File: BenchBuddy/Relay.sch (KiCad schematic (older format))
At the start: 0 parts

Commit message: Week3 part 1
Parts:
- added D?: LED, ~, symbol LED
- added D?: DIODE, ~, symbol DIODE
- added K?: RELAY_SPDT, ~, symbol RELAY_SPDT
- added Q?: NPN, ~, symbol NPN
- added R? (x5): R, ~, symbol R
- added U?: PHTRANS, ~, symbol PHTRANS
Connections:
- net DIN+: now also U?.1
- net DIN-: now also R?.1
- new net: R?.2, U?.2
- new net: D?.1 (A), R?.1, U?.4
- new net: R?.1, U?.6
- new net: Q?.1 (E), R?.1
- new net: Q?.2 (B), R?.2
- new net: D?.1 (A), K?.5 (COIL_-), Q?.3 (C)
- new net: D?.2 (K), R?.1
- new net +12P: D?.2 (K), K?.2 (COIL_+), R?.2, U?.5
- new net COM: K?.1 (COM)
- new net GND: R?.2, R?.2
- new net NC: K?.4 (NC)
- new net NO: K?.3 (NO)
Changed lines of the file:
@@
 $Descr A4 11693 8268
 encoding utf-8
-Sheet 4 8
+Sheet 4 9
 Title ""
-Date "1 feb 2014"
+Date "5 mar 2014"
 Rev ""
 Comp ""
@@
 Comment4 ""
 $EndDescr
-Text HLabel 1100 1400 0    60   Input ~ 0
+Text HLabel 1550 3050 0    60   Input ~ 0
 DIN+
-Text HLabel 1100 1700 0    60   Output ~ 0
+Text HLabel 1550 3400 0    60   Output ~ 0
 DIN-
-Text HLabel 9850 1650 0    60   Input ~ 0
-Relay+
-Text HLabel 9850 1900 0    60   Output ~ 0
-Relay-
+Text HLabel 9450 1800 2    60   BiDi ~ 0
+NC
+Text HLabel 9450 2000 2    60   BiDi ~ 0
+NO
+$Comp
+L PHTRANS U?
+U 1 1 53162E90
+P 4200 3250
+F 0 "U?" H 4150 3600 70  0000 C CNN
+F 1 "PHTRANS" H 4150 2900 70  0000 C CNN
+F 2 "~" H 4200 3250 60  0000 C CNN
+F 3 "~" H 4200 3250 60  0000 C CNN
+	1    4200 3250
+	1    0    0    -1
+$EndComp
+$Comp
+L NPN Q?
+U 1 1 53162E9F
+P 8000 3450
+F 0 "Q?" H 8000 3300 50  0000 R CNN
+F 1 "NPN" H 8000 3600 50  0000 R CNN
+F 2 "~" H 8000 3450 60  0000 C CNN
+F 3 "~" H 8000 3450 60  0000 C CNN
+	1    8000 3450
+	1    0    0    -1
+$EndComp
+$Comp
+L R R?
+U 1 1 53162EAE
+P 5850 3450
+F 0 "R?" V 5930 3450 40  0000 C CNN
+F 1 "R" V 5857 3451 40  0000 C CNN
+F 2 "~" V 5780 3450 30  0000 C CNN
+F 3 "~" H 5850 3450 30  0000 C CNN
+	1    5850 3450
+	0    -1   -1   0
+$EndComp
+$Comp
+L LED D?
+U 1 1 53162ECC
+P 5250 3750
+F 0 "D?" H 5250 3850 50  0000 C CNN
+F 1 "LED" H 5250 3650 50  0000 C CNN
+F 2 "~" H 5250 3750 60  0000 C CNN
+F 3 "~" H 5250 3750 60  0000 C CNN
+	1    5250 3750
+	0    1    1    0
+$EndComp
+$Comp
+L RELAY_SPDT K?
+U 1 1 5316363E
+P 8700 1850
+F 0 "K?" H 8700 2100 70  0000 C CNN
+F 1 "RELAY_SPDT" H 8700 1300 70  0000 C CNN
+F 2 "~" H 8700 1850 60  0000 C CNN
+F 3 "~" H 8700 1850 60  0000 C CNN
+	1    8700 1850
+	1    0    0    -1
+$EndComp
+Text HLabel 9500 1400 2    60   BiDi ~ 0
+COM
+Wire Wire Line
+	9100 1800 9450 1800
+Wire Wire Line
+	9450 2000 9100 2000
+$Comp
+L R R?
+U 1 1 53163662
+P 8100 4300
+F 0 "R?" V 8180 4300 40  0000 C CNN
+F 1 "R" V 8107 4301 40  0000 C CNN
+F 2 "~" V 8030 4300 30  0000 C CNN
+F 3 "~" H 8100 4300 30  0000 C CNN
+	1    8100 4300
+	1    0    0    -1
+$EndComp
+Wire Wire Line
+	4750 3450 5600 3450
+Wire Wire Line
+	6100 3450 7800 3450
+Wire Wire Line
+	8100 3650 8100 4050
+$Comp
+L GND #PWR?
+U 1 1 531636AD
+P 8100 4800
+F 0 "#PWR?" H 8100 4800 30  0001 C CNN
+F 1 "GND" H 8100 4730 30  0001 C CNN
+F 2 "" H 8100 4800 60  0000 C CNN
+F 3 "" H 8100 4800 60  0000 C CNN
+	1    8100 4800
+	1    0    0    -1
+$EndComp
+Wire Wire Line
+	8100 4550 8100 4800
+$Comp
+L R R?
+U 1 1 531636E0
+P 5250 4300
+F 0 "R?" V 5330 4300 40  0000 C CNN
+F 1 "R" V 5257 4301 40  0000 C CNN
+F 2 "~" V 5180 4300 30  0000 C CNN
+F 3 "~" H 5250 4300 30  0000 C CNN
+	1    5250 4300
+	1    0    0    -1
+$EndComp
+Wire Wire Line
+	5250 3550 5250 3450
+Connection ~ 5250 3450
+Wire Wire Line
+	5250 3950 5250 4050
+Wire Wire Line
+	5250 4550 5250 4700
+Wire Wire Line
+	5250 4700 8100 4700
+Connection ~ 8100 4700
+$Comp
+L +12P #PWR?
+U 1 1 53163718
+P 6200 1400
+F 0 "#PWR?" H 6200 1370 30  0001 C CNN
+F 1 "+12P" H 6200 1500 30  0000 C CNN
+F 2 "" H 6200 1400 60  0000 C CNN
+F 3 "" H 6200 1400 60  0000 C CNN
+	1    6200 1400
+	1    0    0    -1
+$EndComp
+$Comp
+L R R?
+U 1 1 53163736
+P 5300 3050
+F 0 "R?" V 5380 3050 40  0000 C CNN
+F 1 "R" V 5307 3051 40  0000 C CNN
+F 2 "~" V 5230 3050 30  0000 C CNN
+F 3 "~" H 5300 3050 30  0000 C CNN
+	1    5300 3050
+	0    -1   -1   0
+$EndComp
+Wire Wire Line
+	4750 3050 5050 3050
+Wire Wire Line
+	5550 3050 6200 3050
+Wire Wire Line
+	6200 1400 6200 3250
+Wire Wire Line
+	6200 3250 4750 3250
+Connection ~ 6200 3050
+$Comp
+L R R?
+U 1 1 531637B3
+P 2900 3400
+F 0 "R?" V 2980 3400 40  0000 C CNN
+F 1 "R" V 2907 3401 40  0000 C CNN
+F 2 "~" V 2830 3400 30  0000 C CNN
+F 3 "~" H 2900 3400 30  0000 C CNN
+	1    2900 3400
+	0    -1   -1   0
+$EndComp
+Wire Wire Line
+	3650 3400 3150 3400
+Wire Wire Line
+	2650 3400 1550 3400
+Wire Wire Line
+	3650 3050 1550 3050
+Wire Wire Line
+	8300 1900 8100 1900
+Wire Wire Line
+	8100 1900 8100 1400
+Wire Wire Line
+	8100 1400 9500 1400
+Wire Wire Line
+	8300 2200 8100 2200
+Wire Wire Line
+	8100 2200 8100 3250
+Wire Wire Line
+	8300 2100 6200 2100
+Connection ~ 6200 2100
+$Comp
+L DIODE D?
+U 1 1 531638FA
+P 7650 2650
+F 0 "D?" H 7650 2750 40  0000 C CNN
+F 1 "DIODE" H 7650 2550 40  0000 C CNN
+F 2 "~" H 7650 2650 60  0000 C CNN
+F 3 "~" H 7650 2650 60  0000 C CNN
+	1    7650 2650
+	0    -1   -1   0
+$EndComp
+Wire Wire Line
+	7650 2100 7650 2450
+Connection ~ 7650 2100
+Wire Wire Line
+	7650 2850 8100 2850
+Connection ~ 8100 2850
 $EndSCHEMATC

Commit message: Week3 Part 2
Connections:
- net COM renamed RELAY_COM
- net DIN+ renamed RELAY+
- net DIN- renamed RELAY-
- net NC renamed RELAY_NC
- net NO renamed RELAY_NO
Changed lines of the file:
@@
 EESchema Schematic File Version 2
+LIBS:BenchBuddy
 LIBS:power
 LIBS:device
@@
 $Descr A4 11693 8268
 encoding utf-8
-Sheet 4 9
+Sheet 9 9
 Title ""
-Date "5 mar 2014"
+Date "7 mar 2014"
 Rev ""
 Comp ""
@@
 $EndDescr
 Text HLabel 1550 3050 0    60   Input ~ 0
-DIN+
+RELAY+
 Text HLabel 1550 3400 0    60   Output ~ 0
-DIN-
+RELAY-
 Text HLabel 9450 1800 2    60   BiDi ~ 0
-NC
+RELAY_NC
 Text HLabel 9450 2000 2    60   BiDi ~ 0
-NO
+RELAY_NO
 $Comp
 L PHTRANS U?
@@
 $EndComp
 Text HLabel 9500 1400 2    60   BiDi ~ 0
-COM
+RELAY_COM
 Wire Wire Line
 	9100 1800 9450 1800

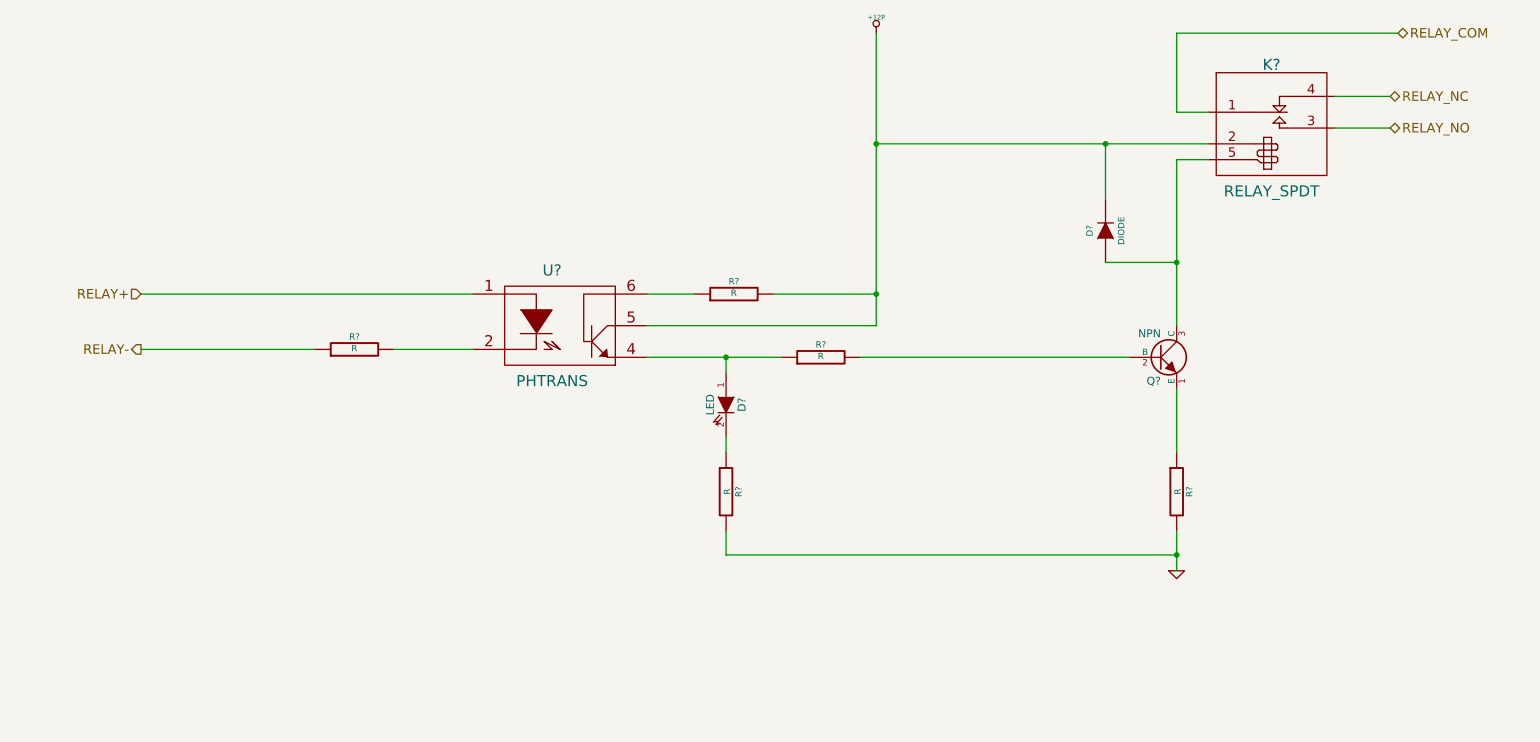
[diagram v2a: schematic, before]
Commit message: Colocação dos Componentes Relé
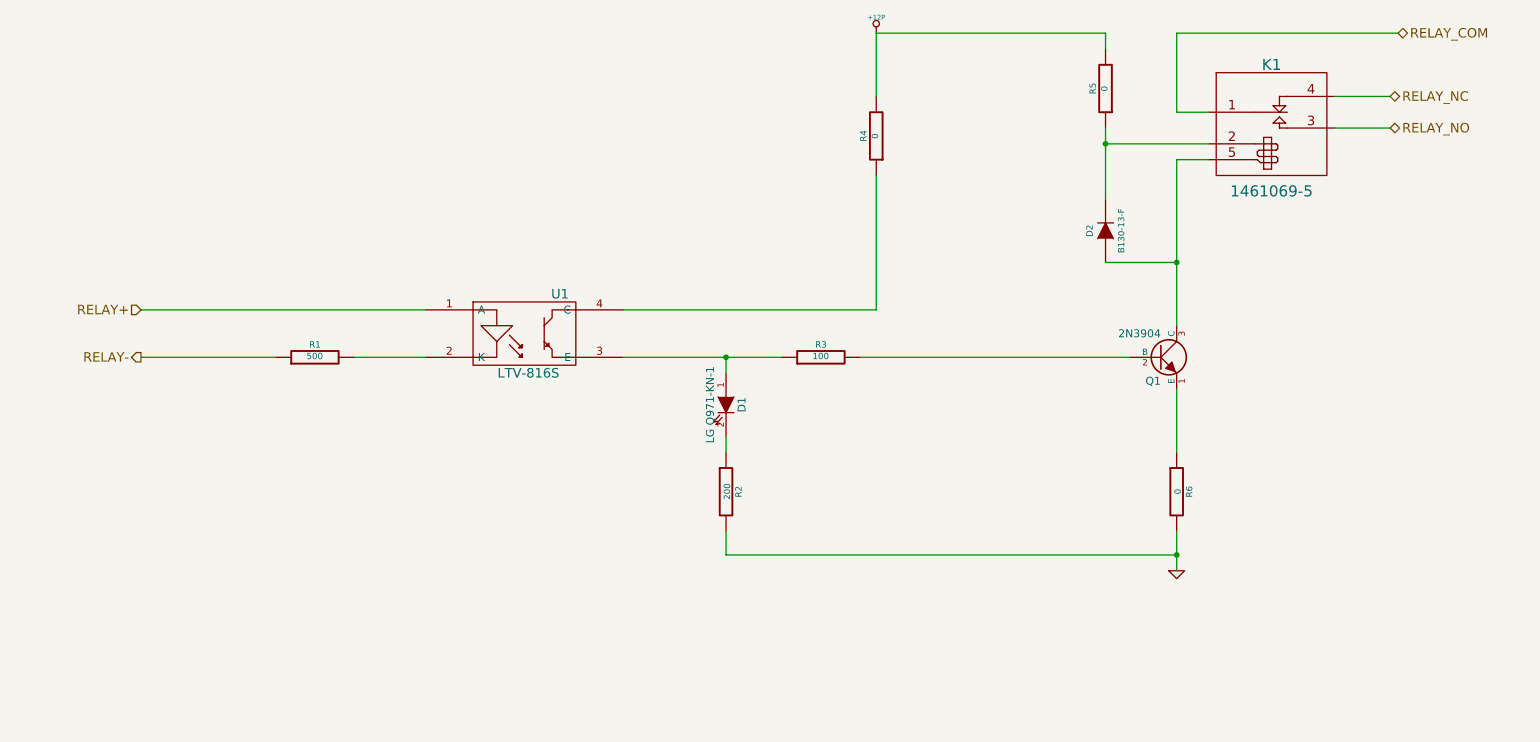
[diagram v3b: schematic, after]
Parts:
- removed R?: R, ~, symbol R
- removed U?: PHTRANS, ~, symbol PHTRANS
- added R4, R5: 0, ~, symbol R
- added U1: LTV-816S, symbol OPTO-TRANSISTOR4
- D1: renamed from D?; value LED -> LG Q971-KN-1
- D2: renamed from D?; value DIODE -> B130-13-F
- K1: renamed from K?; value RELAY_SPDT -> 1461069-5
- Q1: renamed from Q?; value NPN -> 2N3904; Distribuitor Part Number (none) -> MMBT3904-FDICT-ND; MFG Name (none) -> Diodes Inc; MFG Part Number (none) -> MMBT3904-7-F
- R1: renamed from R?; value R -> 500
- R2: renamed from R?; value R -> 200
- R3: renamed from R?; value R -> 100
- R6: renamed from R?; value R -> 0
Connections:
- net +12P: now also R4.2, R5.2; no longer D2.2 (K), K1.2 (COIL_+)
- net RELAY+: now also U1.1 (A)
- net at R1.2: now also U1.2 (K)
- net at D1.1 (A), R3.1: now also U1.3 (E)
- new net: D2.2 (K), K1.2 (COIL_+), R5.1
- new net: R4.1, U1.4 (C)
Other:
- moved on the sheet: R1
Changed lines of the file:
@@
 $Descr A4 11693 8268
 encoding utf-8
-Sheet 9 9
+Sheet 8 9
 Title ""
-Date "7 mar 2014"
+Date "9 mar 2014"
 Rev ""
 Comp ""
@@
 Comment4 ""
 $EndDescr
-Text HLabel 1550 3050 0    60   Input ~ 0
+Text HLabel 1550 3150 0    60   Input ~ 0
 RELAY+
-Text HLabel 1550 3400 0    60   Output ~ 0
+Text HLabel 1550 3450 0    60   Output ~ 0
 RELAY-
 Text HLabel 9450 1800 2    60   BiDi ~ 0
@@
 RELAY_NO
 $Comp
-L PHTRANS U?
-U 1 1 53162E90
-P 4200 3250
-F 0 "U?" H 4150 3600 70  0000 C CNN
-F 1 "PHTRANS" H 4150 2900 70  0000 C CNN
-F 2 "~" H 4200 3250 60  0000 C CNN
-F 3 "~" H 4200 3250 60  0000 C CNN
-	1    4200 3250
-	1    0    0    -1
-$EndComp
-$Comp
-L NPN Q?
+L NPN Q1
 U 1 1 53162E9F
 P 8000 3450
-F 0 "Q?" H 8000 3300 50  0000 R CNN
-F 1 "NPN" H 8000 3600 50  0000 R CNN
+F 0 "Q1" H 8000 3300 50  0000 R CNN
+F 1 "2N3904" H 8000 3600 50  0000 R CNN
 F 2 "~" H 8000 3450 60  0000 C CNN
 F 3 "~" H 8000 3450 60  0000 C CNN
+F 4 "Diodes Inc" H 8000 3450 60  0001 C CNN "MFG Name"
+F 5 "MMBT3904-7-F" H 8000 3450 60  0001 C CNN "MFG Part Number"
+F 6 "MMBT3904-FDICT-ND" H 8000 3450 60  0001 C CNN "Distribuitor Part Number"
 	1    8000 3450
 	1    0    0    -1
 $EndComp
 $Comp
-L R R?
+L R R3
 U 1 1 53162EAE
 P 5850 3450
-F 0 "R?" V 5930 3450 40  0000 C CNN
-F 1 "R" V 5857 3451 40  0000 C CNN
+F 0 "R3" V 5930 3450 40  0000 C CNN
+F 1 "100" V 5857 3451 40  0000 C CNN
 F 2 "~" V 5780 3450 30  0000 C CNN
 F 3 "~" H 5850 3450 30  0000 C CNN
@@
 $EndComp
 $Comp
-L LED D?
+L LED D1
 U 1 1 53162ECC
 P 5250 3750
-F 0 "D?" H 5250 3850 50  0000 C CNN
-F 1 "LED" H 5250 3650 50  0000 C CNN
+F 0 "D1" H 5250 3850 50  0000 C CNN
+F 1 "LG Q971-KN-1" H 5250 3650 50  0000 C CNN
 F 2 "~" H 5250 3750 60  0000 C CNN
 F 3 "~" H 5250 3750 60  0000 C CNN
@@
 $EndComp
 $Comp
-L RELAY_SPDT K?
+L RELAY_SPDT K1
 U 1 1 5316363E
 P 8700 1850
-F 0 "K?" H 8700 2100 70  0000 C CNN
-F 1 "RELAY_SPDT" H 8700 1300 70  0000 C CNN
+F 0 "K1" H 8700 2100 70  0000 C CNN
+F 1 "1461069-5" H 8700 1300 70  0000 C CNN
 F 2 "~" H 8700 1850 60  0000 C CNN
 F 3 "~" H 8700 1850 60  0000 C CNN
@@
 	9450 2000 9100 2000
 $Comp
-L R R?
+L R R6
 U 1 1 53163662
 P 8100 4300
-F 0 "R?" V 8180 4300 40  0000 C CNN
-F 1 "R" V 8107 4301 40  0000 C CNN
+F 0 "R6" V 8180 4300 40  0000 C CNN
+F 1 "0" V 8107 4301 40  0000 C CNN
 F 2 "~" V 8030 4300 30  0000 C CNN
 F 3 "~" H 8100 4300 30  0000 C CNN
@@
 $EndComp
 Wire Wire Line
-	4750 3450 5600 3450
+	4600 3450 5600 3450
 Wire Wire Line
 	6100 3450 7800 3450
@@
 	8100 3650 8100 4050
 $Comp
-L GND #PWR?
+L GND #PWR49
 U 1 1 531636AD
 P 8100 4800
-F 0 "#PWR?" H 8100 4800 30  0001 C CNN
+F 0 "#PWR49" H 8100 4800 30  0001 C CNN
 F 1 "GND" H 8100 4730 30  0001 C CNN
 F 2 "" H 8100 4800 60  0000 C CNN
@@
 	8100 4550 8100 4800
 $Comp
-L R R?
+L R R2
 U 1 1 531636E0
 P 5250 4300
-F 0 "R?" V 5330 4300 40  0000 C CNN
-F 1 "R" V 5257 4301 40  0000 C CNN
+F 0 "R2" V 5330 4300 40  0000 C CNN
+F 1 "200" V 5257 4301 40  0000 C CNN
 F 2 "~" V 5180 4300 30  0000 C CNN
 F 3 "~" H 5250 4300 30  0000 C CNN
@@
 Connection ~ 8100 4700
 $Comp
-L +12P #PWR?
+L +12P #PWR48
 U 1 1 53163718
 P 6200 1400
-F 0 "#PWR?" H 6200 1370 30  0001 C CNN
+F 0 "#PWR48" H 6200 1370 30  0001 C CNN
 F 1 "+12P" H 6200 1500 30  0000 C CNN
 F 2 "" H 6200 1400 60  0000 C CNN
@@
 	1    0    0    -1
 $EndComp
-$Comp
-L R R?
-U 1 1 53163736
-P 5300 3050
-F 0 "R?" V 5380 3050 40  0000 C CNN
-F 1 "R" V 5307 3051 40  0000 C CNN
-F 2 "~" V 5230 3050 30  0000 C CNN
-F 3 "~" H 5300 3050 30  0000 C CNN
-	1    5300 3050
+Wire Wire Line
+	4600 3150 6200 3150
+$Comp
+L R R1
+U 1 1 531637B3
+P 2650 3450
+F 0 "R1" V 2730 3450 40  0000 C CNN
+F 1 "500" V 2657 3451 40  0000 C CNN
+F 2 "~" V 2580 3450 30  0000 C CNN
+F 3 "~" H 2650 3450 30  0000 C CNN
+	1    2650 3450
 	0    -1   -1   0
 $EndComp
 Wire Wire Line
-	4750 3050 5050 3050
-Wire Wire Line
-	5550 3050 6200 3050
-Wire Wire Line
-	6200 1400 6200 3250
-Wire Wire Line
-	6200 3250 4750 3250
-Connection ~ 6200 3050
-$Comp
-L R R?
-U 1 1 531637B3
-P 2900 3400
-F 0 "R?" V 2980 3400 40  0000 C CNN
-F 1 "R" V 2907 3401 40  0000 C CNN
-F 2 "~" V 2830 3400 30  0000 C CNN
-F 3 "~" H 2900 3400 30  0000 C CNN
-	1    2900 3400
-	0    -1   -1   0
-$EndComp
-Wire Wire Line
-	3650 3400 3150 3400
-Wire Wire Line
-	2650 3400 1550 3400
-Wire Wire Line
-	3650 3050 1550 3050
+	2400 3450 1550 3450
 Wire Wire Line
 	8300 1900 8100 1900
@@
 Wire Wire Line
 	8100 2200 8100 3250
-Wire Wire Line
-	8300 2100 6200 2100
-Connection ~ 6200 2100
-$Comp
-L DIODE D?
+$Comp
+L DIODE D2
 U 1 1 531638FA
 P 7650 2650
-F 0 "D?" H 7650 2750 40  0000 C CNN
-F 1 "DIODE" H 7650 2550 40  0000 C CNN
+F 0 "D2" H 7650 2750 40  0000 C CNN
+F 1 "B130-13-F" H 7650 2550 40  0000 C CNN
 F 2 "~" H 7650 2650 60  0000 C CNN
 F 3 "~" H 7650 2650 60  0000 C CNN
@@
 $EndComp
 Wire Wire Line
-	7650 2100 7650 2450
-Connection ~ 7650 2100
+	7650 2000 7650 2450
 Wire Wire Line
 	7650 2850 8100 2850
 Connection ~ 8100 2850
+$Comp
+L OPTO-TRANSISTOR4 U1
+U 1 1 531CD000
+P 4000 3300
+F 0 "U1" H 4200 3550 60  0000 C CNN
+F 1 "LTV-816S" H 4000 3050 60  0000 C CNN
+F 2 "" H 4000 3300 60  0000 C CNN
+F 3 "" H 4000 3300 60  0000 C CNN
+F 4 "TE Connectivity" H 4000 3300 60  0001 C CNN "MFG Name"
+F 5 "LTV-816S" H 4000 3300 60  0001 C CNN "MFG Part Number"
+F 6 "PB1321-ND" H 4000 3300 60  0001 C CNN "Distribuitor Part Number"
+	1    4000 3300
+	1    0    0    -1
+$EndComp
+Wire Wire Line
+	2900 3450 3350 3450
+Wire Wire Line
+	3350 3150 1550 3150
+Wire Wire Line
+	8300 2100 7650 2100
+$Comp
+L R R4
+U 1 1 531CD647
+P 6200 2050
+F 0 "R4" V 6280 2050 40  0000 C CNN
+F 1 "0" V 6207 2051 40  0000 C CNN
+F 2 "~" V 6130 2050 30  0000 C CNN
+F 3 "~" H 6200 2050 30  0000 C CNN
+	1    6200 2050
+	-1   0    0    1
+$EndComp
+$Comp
+L R R5
+U 1 1 531CD64D
+P 7650 1750
+F 0 "R5" V 7730 1750 40  0000 C CNN
+F 1 "0" V 7657 1751 40  0000 C CNN
+F 2 "~" V 7580 1750 30  0000 C CNN
+F 3 "~" H 7650 1750 30  0000 C CNN
+	1    7650 1750
+	-1   0    0    1
+$EndComp
+Wire Wire Line
+	6200 3150 6200 2300
+Wire Wire Line
+	6200 1800 6200 1400
+Connection ~ 7650 2100
+Wire Wire Line
+	7650 1500 7650 1400
+Wire Wire Line
+	7650 1400 6200 1400
 $EndSCHEMATC

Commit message: Pre layout
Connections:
- net RELAY_NC: now also K1.3 (NO); no longer K1.4 (NC)
- net RELAY_NO: now also K1.4 (NC); no longer K1.3 (NO)
- net GND renamed GND_RELAY
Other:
- moved on the sheet: D1, D2, K1, Q1, R1, R2, R3, R4, R5, R6, U1

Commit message: Pre layout 2
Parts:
- R1: value 500 -> 200
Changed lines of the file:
@@
 Sheet 6 9
 Title ""
-Date "30 mar 2014"
+Date "23 apr 2014"
 Rev ""
 Comp ""
@@
 Connection ~ 8250 5600
 $Comp
-L +12P #PWR034
+L +12P #PWR035
 U 1 1 53163718
 P 6350 2300
-F 0 "#PWR034" H 6350 2270 30  0001 C CNN
+F 0 "#PWR035" H 6350 2270 30  0001 C CNN
 F 1 "+12P" H 6350 2400 30  0000 C CNN
 F 2 "" H 6350 2300 60  0000 C CNN
@@
 P 2800 4350
 F 0 "R1" V 2880 4350 40  0000 C CNN
-F 1 "500" V 2807 4351 40  0000 C CNN
+F 1 "200" V 2807 4351 40  0000 C CNN
 F 2 "~" V 2730 4350 30  0000 C CNN
 F 3 "~" H 2800 4350 30  0000 C CNN
@@
 	7800 2300 6350 2300
 $Comp
-L GND_RELAY #PWR035
+L GND_RELAY #PWR036
 U 1 1 53370BA0
 P 8250 5700
-F 0 "#PWR035" H 8250 5700 30  0001 C CNN
+F 0 "#PWR036" H 8250 5700 30  0001 C CNN
 F 1 "GND_RELAY" H 8250 5630 30  0000 C CNN
 F 2 "~" H 8250 5700 60  0000 C CNN
